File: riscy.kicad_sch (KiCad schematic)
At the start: 38 parts, among them J1 Conn_01x15_Pin, J2 Conn_01x15_Pin, J3 USB_C_Receptacle_USB2.0_14P, Q1 MMBT2222A, Q2 MMBT2222A, SW1 SW_Push, SW2 SW_Push, U2 FT231XS, U3 ESP32-C3-WROOM-02, U4 AMS1117-3.3

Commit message: updated schematicss
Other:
- note added: "Sphuro"
- company: sphuro -> (none)
- title: (none) -> Risk 5 based development board
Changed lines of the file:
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@@
 	(paper "A3")
 	(title_block
+		(title "Risk 5 based development board")
 		(date "7/01/25")
-		(company "sphuro")
 	)
 	(junction
@@
 		(effects
 			(font
-				(face "JetBrains Mono SemiBold")
+				(face "JetBrainsMono NF Medium")
 				(size 2.54 2.54)
 				(color 101 200 99 1)
@@
 			)
 		)
+	)
+	(text "Sphuro"
+		(exclude_from_sim no)
+		(at 325.374 262.89 0)
+		(effects
+			(font
+				(face "HeavyData Nerd Font")
+				(size 10.16 10.16)
+				(color 59 142 217 1)
+			)
+		)

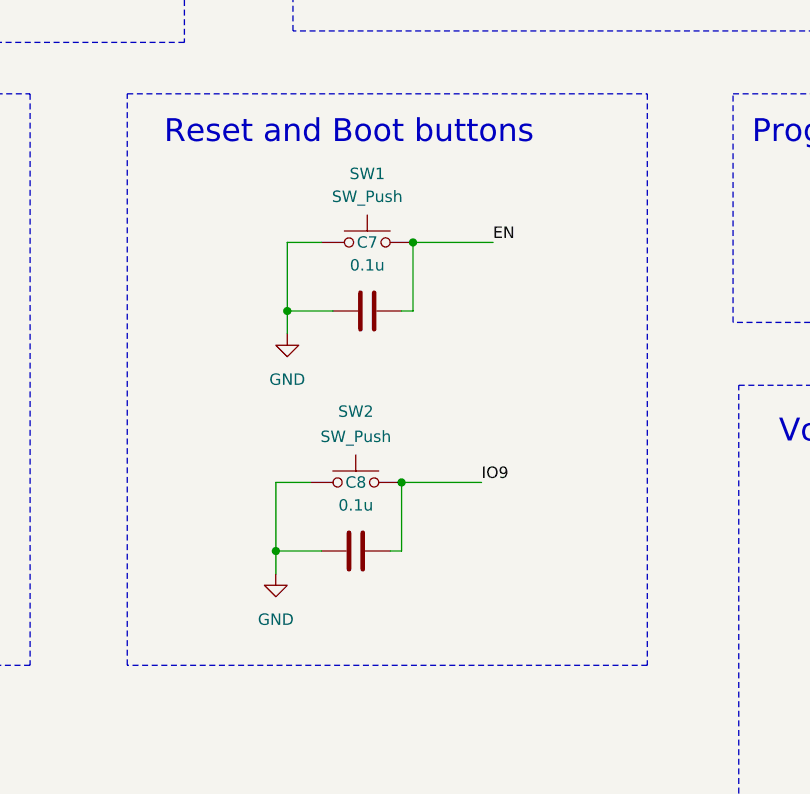
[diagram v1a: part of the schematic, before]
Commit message: added switch footprints
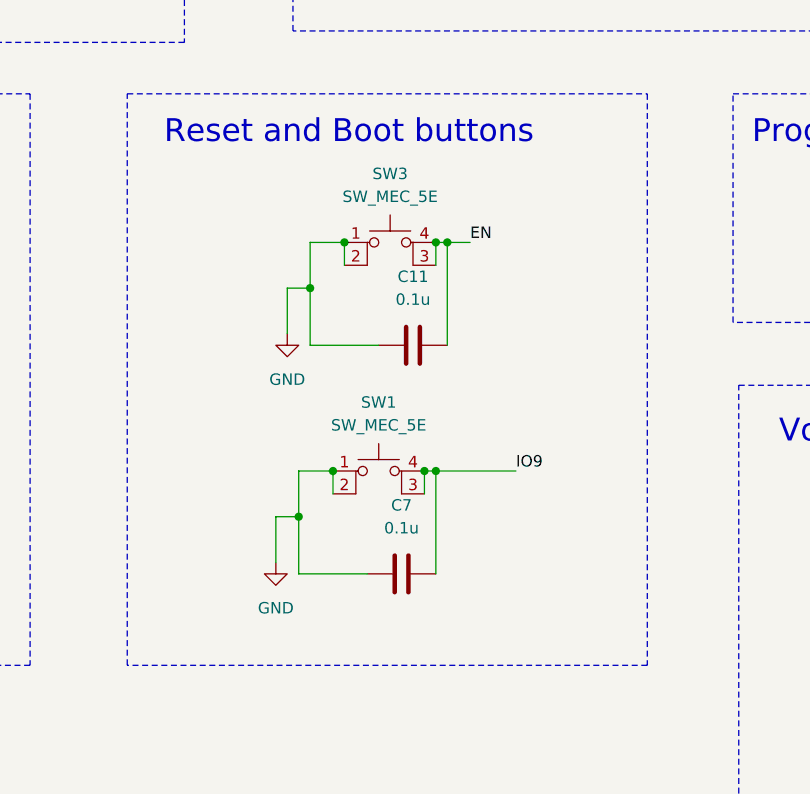
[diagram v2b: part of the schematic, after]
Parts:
- removed C8: 0.1u, Capacitor_SMD:C_0603_1608Metric, symbol Device:C
- removed SW1, SW2: SW_Push, symbol Switch:SW_Push
- added C11: 0.1u, Capacitor_SMD:C_0603_1608Metric, symbol Device:C
- added SW1, SW3: SW_MEC_5E, sources:SW_VS-1213-67-160GF, symbol Switch:SW_MEC_5E
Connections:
- net EN: now also C11.2, SW3.3 (K), SW3.4 (A); no longer C7.2
- net GND: now also C11.1, SW1.1, SW1.2, SW3.1, SW3.2
- net IO9: now also C7.2, SW1.3 (K), SW1.4 (A)

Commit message: shcematic completed now to the pcb design:)
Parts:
- SW1, SW3: footprint sources:SW_VS-1213-67-160GF -> sources:SW_1825910-6-4
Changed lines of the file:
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@@
 			)
 		)
-		(property "Footprint" "sources:SW_VS-1213-67-160GF"
+		(property "Footprint" "sources:SW_1825910-6-4"
 			(at 260.35 119.38 0)
 			(effects
@@
 			)
 		)
-		(property "Footprint" "sources:SW_VS-1213-67-160GF"
+		(property "Footprint" "sources:SW_1825910-6-4"
 			(at 259.08 144.78 0)
 			(effects
